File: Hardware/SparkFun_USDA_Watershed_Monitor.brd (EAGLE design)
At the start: 63.5 x 63.5 mm, 250 parts, among them J10 QWIIC_RIGHT_ANGLE, J12 3-PIN SMD, J3 QWIIC_RIGHT_ANGLE, J4 U.FL, J5 RJ45, J7 RJ45, J9 RJ45, Q1 20V/4.2A/52mΩ/1.4W, Q10 20V/4.2A/52mΩ/1.4W, Q11 20V/0.2A/8MHz/1.2Ω/1Vth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

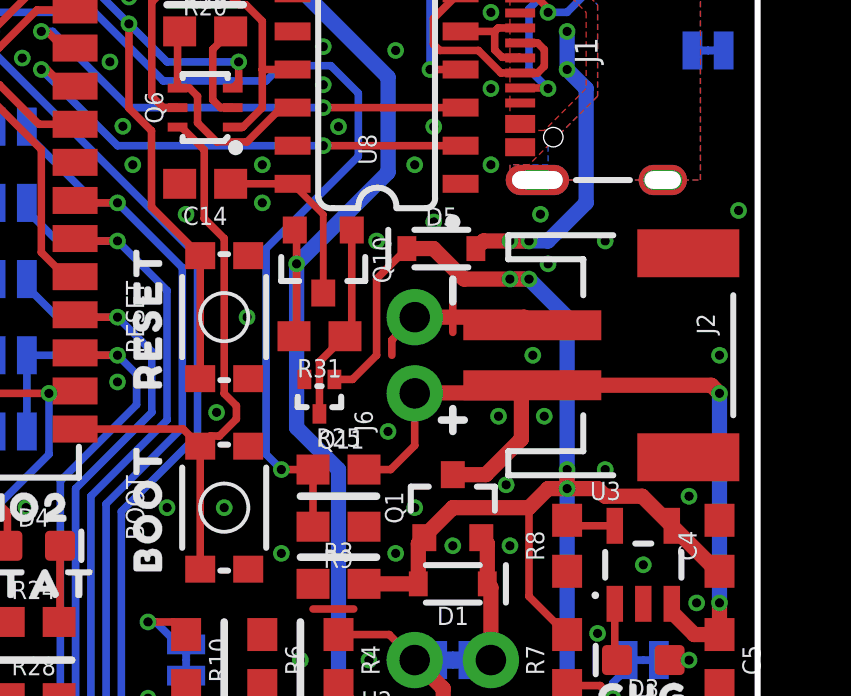
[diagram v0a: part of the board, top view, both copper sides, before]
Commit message: Flip and nudge CH340 power control components
Again...
Gives more clearance between components and pads
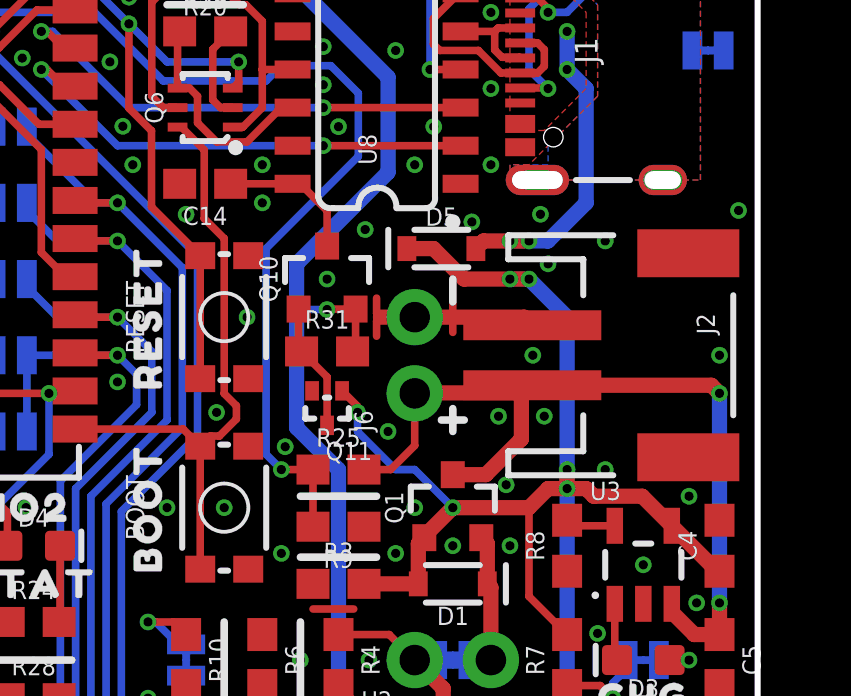
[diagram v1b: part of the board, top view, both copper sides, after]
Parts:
- moved U$21 3.81 mm to (54.0, 41.9)
- moved Q10 0.65 mm to (49.1, 44.5), turned to 0 degrees
- moved R31 0.57 mm to (49.1, 42.0), turned to 0 degrees
- moved Q11 0.46 mm to (49.1, 39.6)
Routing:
- net N$31: track 6.58 -> 4.27 mm
- net N$32: track 6.13 -> 4.76 mm
- net GND: track 28.9 -> 29.8 mm, vias 289 -> 291
- net 5V: track 54.5 -> 54.6 mm, vias 4 -> 6

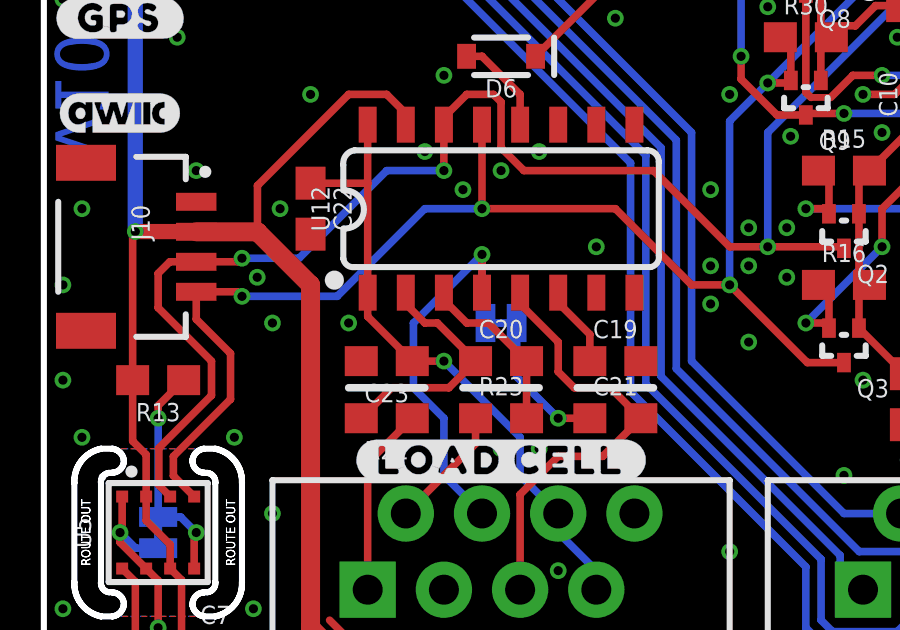
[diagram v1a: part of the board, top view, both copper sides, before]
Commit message: Reorient CAP jumper label
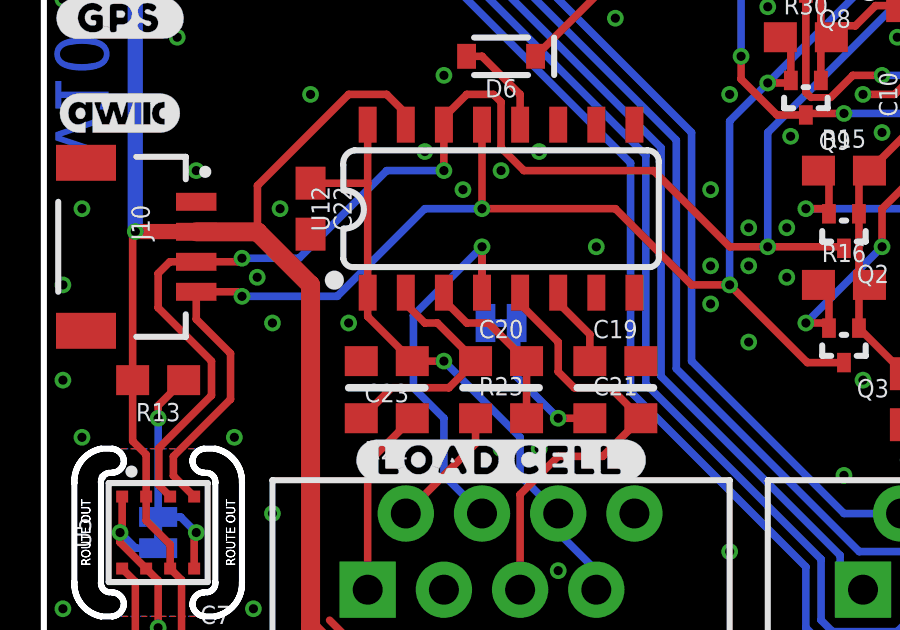
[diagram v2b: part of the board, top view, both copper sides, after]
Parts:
- moved U$17 2.43 mm to (15.2, 19.4), turned to 0 degrees
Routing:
- net NAU_B-: track 14.1 -> 14.9 mm
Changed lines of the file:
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@@
 <element name="U$15" library="output" package="#I2C#0" value="" x="54.61" y="16.891" smashed="yes" rot="MR0"/>
 <element name="U$16" library="output" package="CHG0" value="" x="59.69" y="30.48" smashed="yes"/>
-<element name="U$17" library="output" package="#CAP#0" value="" x="13.462" y="17.78" smashed="yes" rot="MR270"/>
+<element name="U$17" library="output" package="#CAP#0" value="" x="15.24" y="19.431" smashed="yes" rot="MR0"/>
 <element name="U$18" library="output" package="#BME_ADR#0" value="" x="3.81" y="11.557" smashed="yes" rot="MR90"/>
 <element name="U$19" library="output" package="#ICM_ADR#0" value="" x="31.75" y="18.161" smashed="yes" rot="MR0"/>
@@
 <contactref element="U12" pad="4"/>
 <contactref element="NAU_CAP" pad="2"/>
-<via x="14.605" y="20.066" extent="1-16" drill="0.3048"/>
-<wire x1="14.605" y1="20.066" x2="14.605" y2="18.79" width="0.254" layer="1"/>
-<wire x1="14.605" y1="20.066" x2="14.605" y2="17.8943" width="0.254" layer="16"/>
+<via x="14.605" y="20.32" extent="1-16" drill="0.3048"/>
+<wire x1="14.605" y1="20.32" x2="14.605" y2="18.79" width="0.254" layer="1"/>
+<wire x1="14.605" y1="20.32" x2="14.605" y2="17.8943" width="0.254" layer="16"/>
 <wire x1="14.605" y1="17.8943" x2="14.7193" y2="17.78" width="0.254" layer="16"/>
 <contactref element="J5" pad="4"/>
-<wire x1="14.605" y1="20.066" x2="12.319" y2="17.78" width="0.254" layer="16"/>
+<wire x1="14.605" y1="20.32" x2="12.319" y2="18.034" width="0.254" layer="16"/>
 <wire x1="13.335" y1="14.605" x2="12.319" y2="15.621" width="0.254" layer="16"/>
-<wire x1="12.319" y1="15.621" x2="12.319" y2="17.78" width="0.254" layer="16"/>
+<wire x1="12.319" y1="15.621" x2="12.319" y2="18.034" width="0.254" layer="16"/>
 <wire x1="13.335" y1="14.605" x2="13.335" y2="12.7" width="0.254" layer="16"/>
 <wire x1="14.605" y1="11.43" x2="13.335" y2="12.7" width="0.254" layer="16"/>

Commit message: Update power LED
Change to new SKU
Set as DNP
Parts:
- D2: value RED -> DNP
- R10: value 1k -> DNP
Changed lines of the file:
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@@
 <attribute name="VALUE" x="59.69" y="32.893" size="0.6096" layer="28" font="vector" ratio="20" rot="MR180" align="top-center"/>
 </element>
-<element name="D2" library="SparkFun-LED" package="LED-0603" value="RED" x="44.45" y="27.94" smashed="yes" rot="R90">
+<element name="D2" library="SparkFun-LED" package="LED-0603" value="DNP" x="44.45" y="27.94" smashed="yes" rot="R90">
 <attribute name="NAME" x="43.815" y="27.94" size="0.6096" layer="25" font="vector" ratio="20" rot="R90" align="bottom-center"/>
-<attribute name="PROD_ID" value="DIO-00819" x="44.45" y="27.94" size="1.778" layer="27" font="vector" ratio="15" rot="R90" display="off"/>
-<attribute name="VALUE" x="45.085" y="27.94" size="0.6096" layer="27" font="vector" ratio="20" rot="R90" align="top-center"/>
+<attribute name="PROD_ID" value="" x="44.45" y="27.94" size="1.778" layer="27" font="vector" ratio="15" rot="R90" display="off"/>
 </element>
 <element name="D3" library="SparkFun-LED" package="LED-0603" value="Yellow" x="59.69" y="31.75" smashed="yes" rot="R180">
@@
 <attribute name="VALUE" x="57.912" y="35.56" size="0.6096" layer="27" font="vector" ratio="20" rot="R90" align="top-center"/>
 </element>
-<element name="R10" library="SparkFun-Resistors" package="0603" value="1k" x="44.45" y="31.75" smashed="yes" rot="R270">
+<element name="R10" library="SparkFun-Resistors" package="0603" value="DNP" x="44.45" y="31.75" smashed="yes" rot="R270">
 <attribute name="NAME" x="45.212" y="31.75" size="0.6096" layer="25" font="vector" ratio="20" rot="R270" align="bottom-center"/>
-<attribute name="PROD_ID" value="RES-07856" x="44.45" y="31.75" size="1.778" layer="27" font="vector" ratio="15" rot="R270" display="off"/>
-<attribute name="VALUE" value="1k" x="43.688" y="31.75" size="0.6096" layer="27" font="vector" ratio="20" rot="R270" align="top-center"/>
+<attribute name="PROD_ID" value="" x="44.45" y="31.75" size="1.778" layer="27" font="vector" ratio="15" rot="R270" display="off"/>
+<attribute name="VALUE" value="4.7k" x="43.688" y="31.75" size="0.6096" layer="27" font="vector" ratio="20" rot="R270" align="top-center"/>
 </element>
 <element name="PWR" library="SparkFun-Jumpers" package="SMT-JUMPER_2_NC_TRACE_SILK" package3d_urn="urn:adsk.eagle:package:39281/1" value="JUMPER-SMT_2_NC_TRACE_SILK" x="44.45" y="31.75" smashed="yes" rot="MR90">

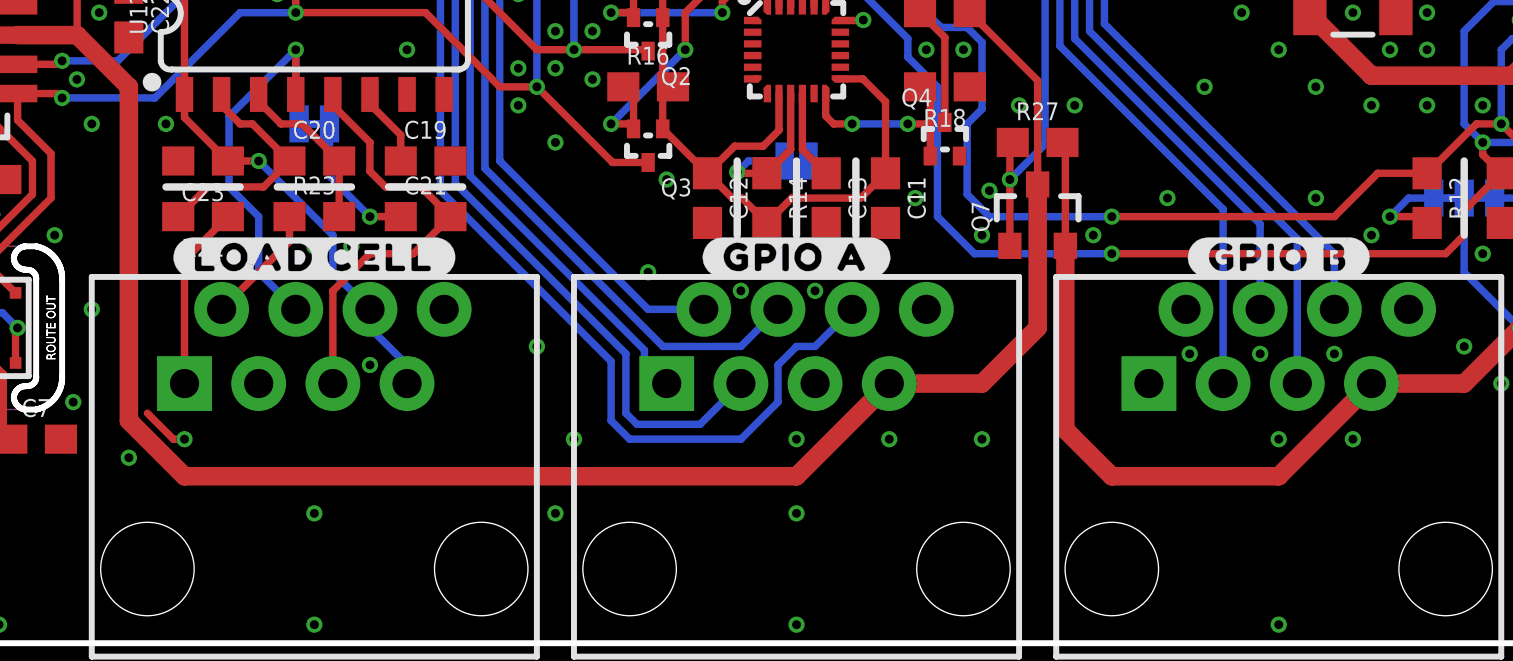
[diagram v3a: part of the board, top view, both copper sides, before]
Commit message: Add 3V3 and VOUT to both RJ45 GPIO connectors
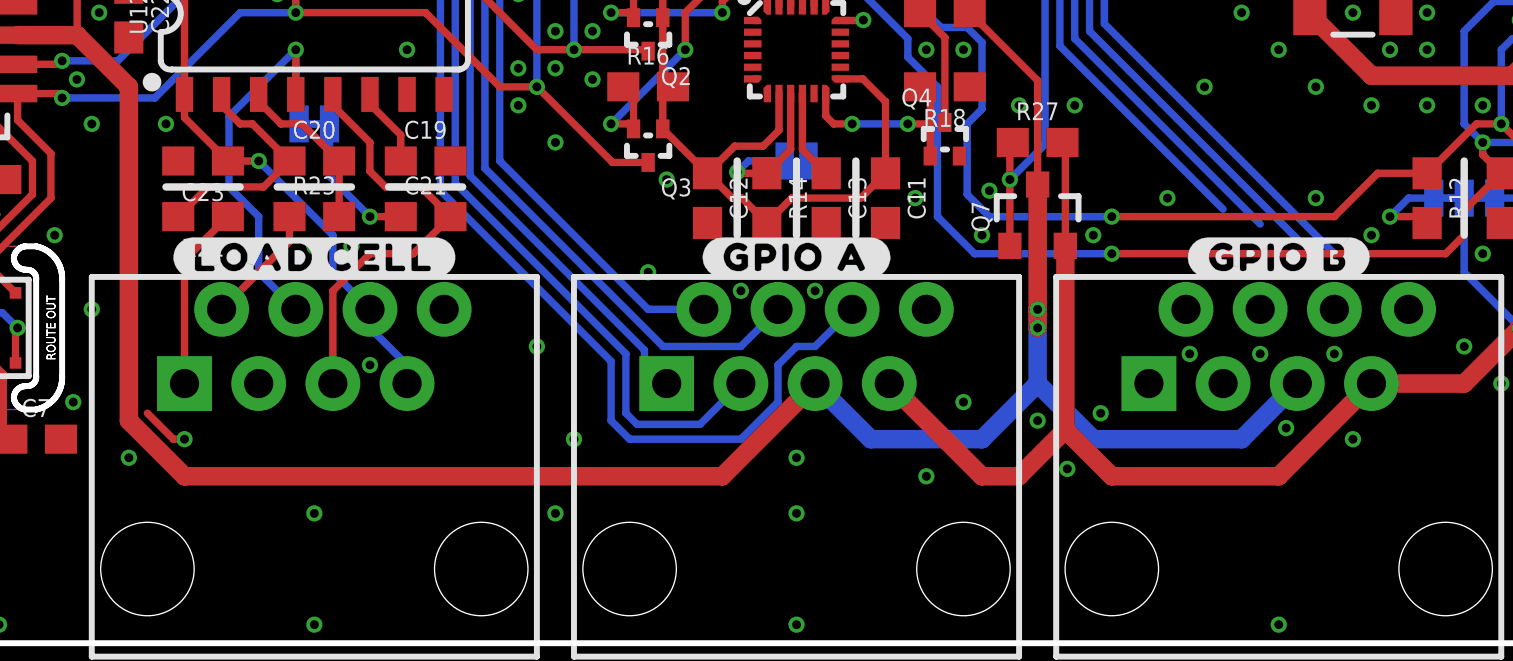
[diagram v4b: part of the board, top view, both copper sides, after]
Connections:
- net 3.3V: now also J7.7
- net ESP_IO17: now also J9.1; no longer J9.3
- net ESP_IO18: now also J9.2; no longer J9.4
- net ESP_IO19: now also J9.3; no longer J9.5
- net ESP_IO23: now also J9.4; no longer J9.6
- net VOUT: now also J7.5, J9.5; no longer J7.7
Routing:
- net VOUT: track 171.3 -> 185.1 mm, vias 3 -> 5
- net 3.3V: track 129.9 -> 137.9 mm
- net ESP_IO17: track 43.3 -> 37.3 mm
- net ESP_IO19: track 48.7 -> 43.7 mm
- net ESP_IO18: track 43.8 -> 40.9 mm
- net ESP_IO23: track 52.0 -> 50.1 mm
- net GND: vias 291 -> 294
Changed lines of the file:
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@@
 <drawing>
 <settings>
-<setting alwaysvectorfont="yes"/>
+<setting alwaysvectorfont="no"/>
 <setting verticaltext="up"/>
 </settings>
@@
 <via x="45.72" y="36.83" extent="1-16" drill="0.3048"/>
 <via x="43.815" y="36.83" extent="1-16" drill="0.3048"/>
-<via x="48.26" y="6.985" extent="1-16" drill="0.3048"/>
+<via x="48.514" y="7.366" extent="1-16" drill="0.3048"/>
 <via x="50.8" y="6.985" extent="1-16" drill="0.3048"/>
 <via x="0.635" y="4.445" extent="1-16" drill="0.3048"/>
@@
 <via x="26.67" y="12.7" extent="1-16" drill="0.3048"/>
 <via x="22.86" y="10.16" extent="1-16" drill="0.3048"/>
-<via x="34.925" y="6.985" extent="1-16" drill="0.3048"/>
-<via x="31.75" y="6.985" extent="1-16" drill="0.3048"/>
+<via x="31.75" y="6.35" extent="1-16" drill="0.3048"/>
 <via x="24.13" y="6.985" extent="1-16" drill="0.3048"/>
 <via x="10.795" y="6.985" extent="1-16" drill="0.3048"/>
@@
 <via x="12.7" y="23.495" extent="1-16" drill="0.3048"/>
 <via x="57.785" y="10.795" extent="1-16" drill="0.3048"/>
-<via x="38.1" y="6.985" extent="1-16" drill="0.3048"/>
 <via x="8.89" y="6.35" extent="1-16" drill="0.3048"/>
 <via x="15.24" y="4.445" extent="1-16" drill="0.3048"/>
@@
 <wire x1="50.8" y1="42.545" x2="50.8" y2="43.053" width="0.254" layer="1"/>
 <via x="47.752" y="38.862" extent="1-16" drill="0.3048"/>
+<via x="40.005" y="7.62" extent="1-16" drill="0.3048"/>
+<via x="37.465" y="8.255" extent="1-16" drill="0.3048"/>
+<via x="36.195" y="5.715" extent="1-16" drill="0.3048"/>
+<via x="41.021" y="5.969" extent="1-16" drill="0.3048"/>
+<via x="42.164" y="7.874" extent="1-16" drill="0.3048"/>
 </signal>
 <signal name="USB_DP">
@@
 <via x="49.149" y="43.434" extent="1-16" drill="0.3048"/>
 <wire x1="49.149" y1="43.434" x2="48.133" y2="43.434" width="0.254" layer="16"/>
+<contactref element="J7" pad="7"/>
+<wire x1="34.925" y1="8.89" x2="38.1" y2="5.715" width="0.635" layer="1"/>
+<wire x1="39.365" y1="5.715" x2="40.955" y2="7.305" width="0.635" layer="1"/>
+<wire x1="38.1" y1="5.715" x2="39.365" y2="5.715" width="0.635" layer="1"/>
 </signal>
 <signal name="N$8">
@@
 <wire x1="40.767" y1="37.465" x2="40.767" y2="20.447" width="0.254" layer="16"/>
 <wire x1="40.767" y1="20.447" x2="46.355" y2="14.859" width="0.254" layer="16"/>
-<contactref element="J9" pad="3"/>
-<wire x1="46.355" y1="14.859" x2="46.355" y2="8.89" width="0.254" layer="16"/>
+<contactref element="J9" pad="1"/>
+<wire x1="43.815" y1="8.89" x2="46.355" y2="14.859" width="0" layer="19" extent="16-16"/>
 </signal>
 <signal name="ESP_IO18">
@@
 <wire x1="41.275" y1="37.211" x2="41.275" y2="20.701" width="0.254" layer="16"/>
 <wire x1="41.275" y1="20.701" x2="47.625" y2="14.351" width="0.254" layer="16"/>
-<contactref element="J9" pad="4"/>
-<wire x1="47.625" y1="14.351" x2="47.625" y2="11.43" width="0.254" layer="16"/>
+<contactref element="J9" pad="2"/>
+<wire x1="45.085" y1="11.43" x2="47.625" y2="14.351" width="0" layer="19" extent="16-16"/>
 </signal>
 <signal name="ESP_IO19">
@@
 <wire x1="41.783" y1="36.957" x2="41.783" y2="20.955" width="0.254" layer="16"/>
 <wire x1="41.783" y1="20.955" x2="48.895" y2="13.843" width="0.254" layer="16"/>
-<contactref element="J9" pad="5"/>
-<wire x1="48.895" y1="13.843" x2="48.895" y2="8.89" width="0.254" layer="16"/>
+<contactref element="J9" pad="3"/>
+<wire x1="46.355" y1="8.89" x2="48.895" y2="13.843" width="0" layer="19" extent="16-16"/>
 </signal>
 <signal name="ESP_IO23">
@@
 <wire x1="44.831" y1="39.243" x2="42.291" y2="36.703" width="0.254" layer="16"/>
 <wire x1="42.291" y1="36.703" x2="42.291" y2="21.209" width="0.254" layer="16"/>
-<contactref element="J9" pad="6"/>
-<wire x1="50.165" y1="13.335" x2="50.165" y2="11.43" width="0.254" layer="16"/>
 <wire x1="42.291" y1="21.209" x2="50.165" y2="13.335" width="0.254" layer="16"/>
+<contactref element="J9" pad="4"/>
+<wire x1="47.625" y1="11.43" x2="50.165" y2="13.335" width="0" layer="19" extent="16-16"/>
 </signal>
 <signal name="ESP_IO25">
@@
 <signal name="VOUT">
 <contactref element="Q7" pad="3"/>
-<wire x1="40.005" y1="15.705" x2="40.005" y2="10.795" width="0.635" layer="1"/>
-<wire x1="40.005" y1="10.795" x2="38.1" y2="8.89" width="0.635" layer="1"/>
-<contactref element="J7" pad="7"/>
-<wire x1="38.1" y1="8.89" x2="34.925" y2="8.89" width="0.635" layer="1"/>
-<wire x1="31.75" y1="5.715" x2="34.925" y2="8.89" width="0.635" layer="1"/>
+<wire x1="40.005" y1="15.705" x2="40.005" y2="11.43" width="0.635" layer="1"/>
+<wire x1="40.005" y1="11.43" x2="40.005" y2="10.795" width="0.635" layer="1"/>
 <wire x1="5.08" y1="20.82" x2="7.12" y2="20.82" width="0.635" layer="1"/>
 <wire x1="8.89" y1="7.62" x2="8.89" y2="19.05" width="0.635" layer="1"/>
@@
 <contactref element="J10" pad="2"/>
 <contactref element="U12" pad="15"/>
-<wire x1="10.795" y1="5.715" x2="31.75" y2="5.715" width="0.635" layer="1"/>
+<wire x1="29.21" y1="5.715" x2="10.795" y2="5.715" width="0.635" layer="1"/>
 <contactref element="J12" pad="3"/>
 <contactref element="U7" pad="3"/>
@@
 <wire x1="26.25" y1="27.305" x2="25.9" y2="27.655" width="0.254" layer="1"/>
 <wire x1="25.9" y1="27.655" x2="25.9" y2="29.929" width="0.254" layer="1"/>
+<contactref element="J7" pad="5"/>
+<contactref element="J9" pad="5"/>
+<wire x1="32.385" y1="8.89" x2="29.21" y2="5.715" width="0.635" layer="1"/>
+<wire x1="48.895" y1="8.89" x2="46.99" y2="6.985" width="0.635" layer="16"/>
+<wire x1="46.99" y1="6.985" x2="41.91" y2="6.985" width="0.635" layer="16"/>
+<wire x1="41.91" y1="6.985" x2="40.005" y2="8.89" width="0.635" layer="16"/>
+<wire x1="40.005" y1="8.89" x2="40.005" y2="10.795" width="0.635" layer="16"/>
+<via x="40.005" y="11.43" extent="1-16" drill="0.3048"/>
+<wire x1="40.005" y1="10.795" x2="40.005" y2="11.43" width="0.635" layer="16"/>
+<via x="40.005" y="10.795" extent="1-16" drill="0.3048"/>
+<wire x1="32.385" y1="8.89" x2="34.29" y2="6.985" width="0.635" layer="16"/>
+<wire x1="38.1" y1="6.985" x2="40.005" y2="8.89" width="0.635" layer="16"/>
+<wire x1="34.29" y1="6.985" x2="38.1" y2="6.985" width="0.635" layer="16"/>
 </signal>
 <signal name="SDA_OUT">
